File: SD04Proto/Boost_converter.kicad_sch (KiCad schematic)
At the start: 2 parts, among them J1 SL_3.5_2_90G3.2_-1605070000, J2 71308-5410

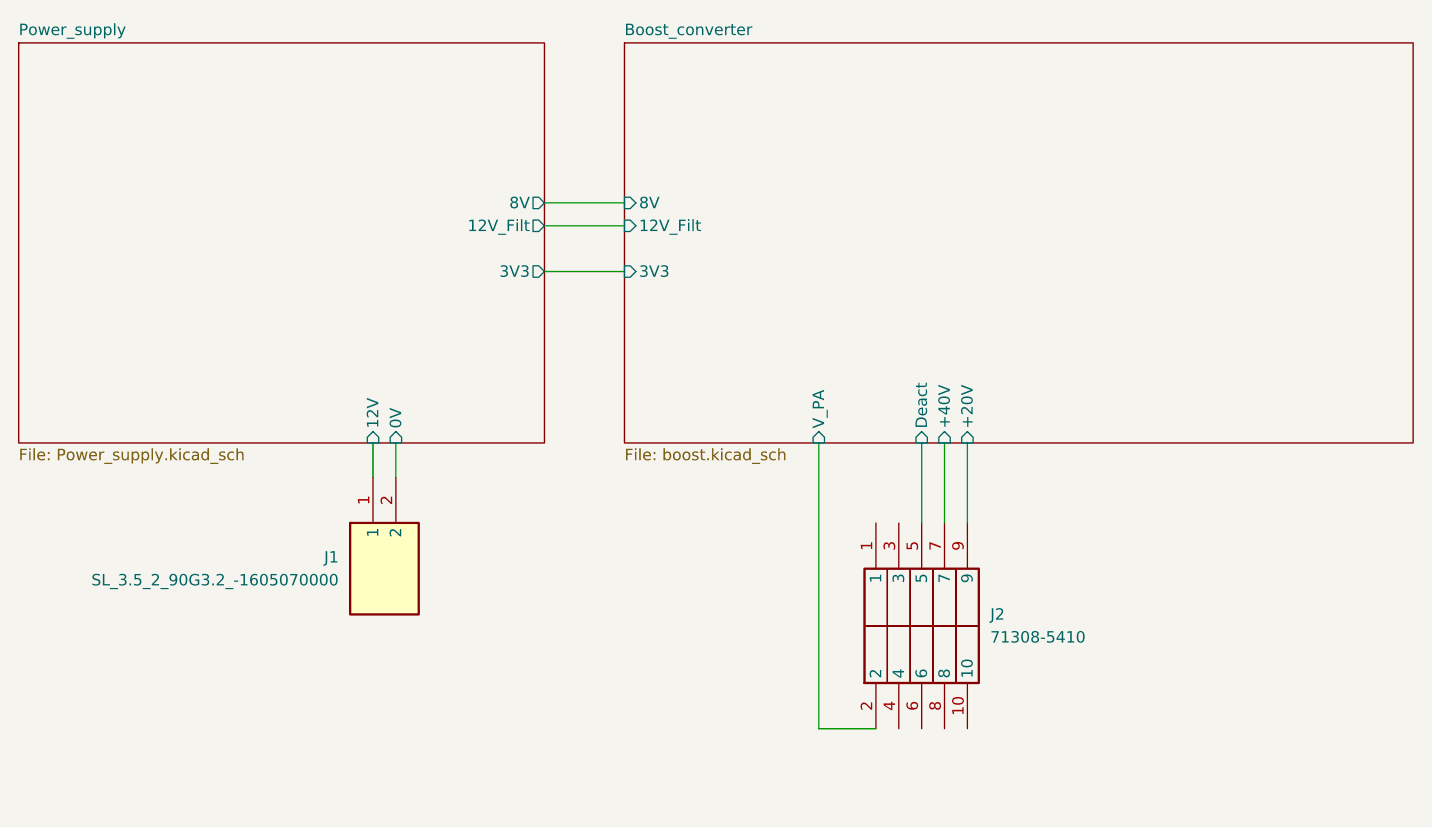
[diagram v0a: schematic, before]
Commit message: changed the layout after review
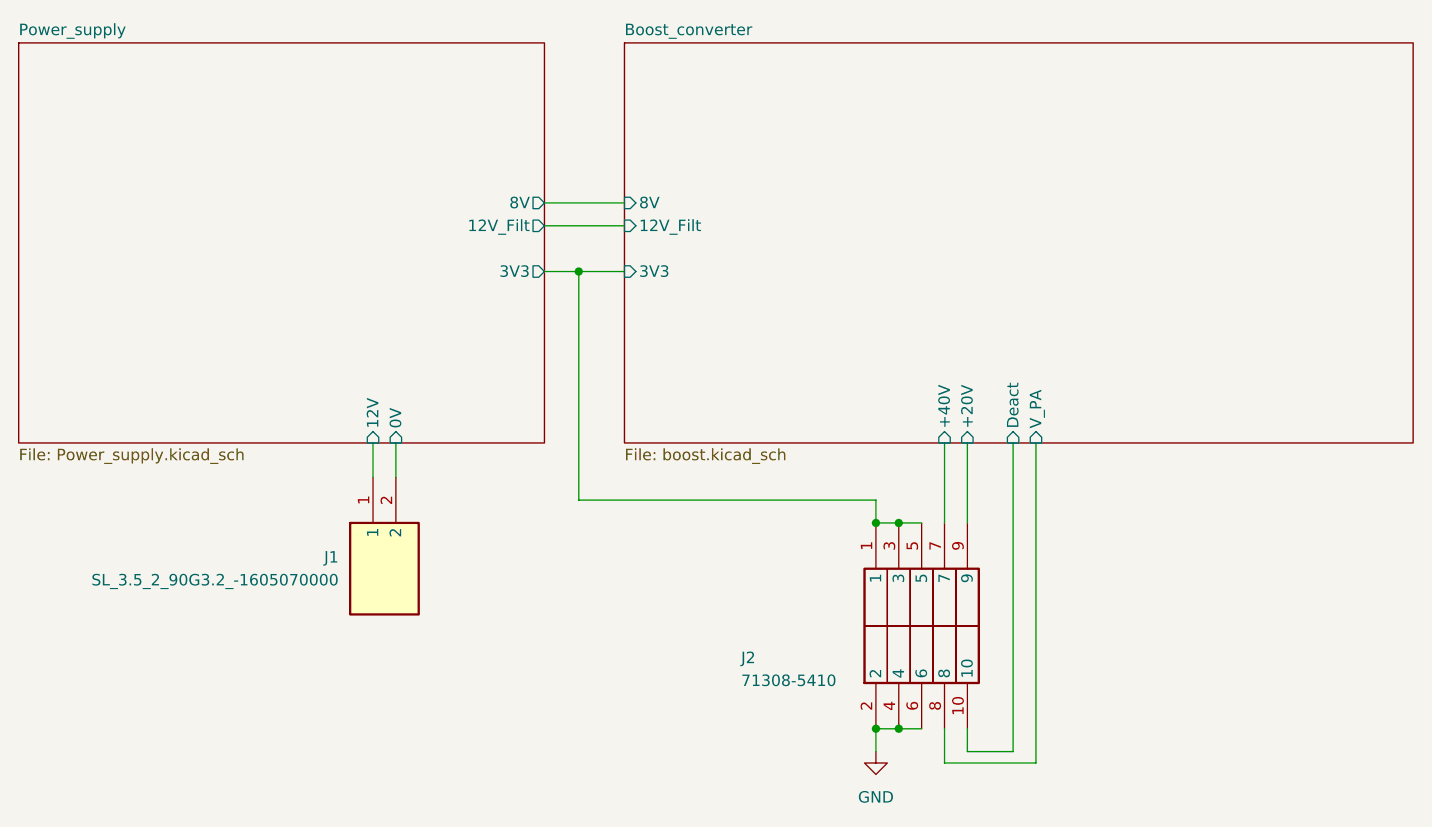
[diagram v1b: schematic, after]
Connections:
- net Boost_converter/3V3: now also J2.1, J2.3, J2.5
- net Boost_converter/Deact: now also J2.10; no longer J2.5
- net Boost_converter/V_PA: now also J2.8; no longer J2.2
- net GND: now reaches J2.4
- net GND: now also J2.2, J2.6
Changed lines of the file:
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@@
 	(generator_version "9.0")
 	(paper "A4")
+	(junction
+		(at 113.03 71.12)
+		(diameter 0)
+		(color 0 0 0 0)
+	)
+	(junction
+		(at 115.57 93.98)
+		(diameter 0)
+		(color 0 0 0 0)
+	)
+	(junction
+		(at 115.57 71.12)
+		(diameter 0)
+		(color 0 0 0 0)
+	)
+	(junction
+		(at 80.01 43.18)
+		(diameter 0)
+		(color 0 0 0 0)
+	)
+	(junction
+		(at 113.03 93.98)
+		(diameter 0)
+		(color 0 0 0 0)
+	)
+	(wire
+		(pts
+			(xy 123.19 96.52) (xy 123.19 93.98)
+		)
+		(stroke
+			(width 0)
+			(type default)
+		)
+	)
+	(wire
+		(pts
+			(xy 115.57 71.12) (xy 118.11 71.12)
+		)
+		(stroke
+			(width 0)
+			(type default)
+		)
+	)
+	(wire
+		(pts
+			(xy 113.03 93.98) (xy 115.57 93.98)
+		)
+		(stroke
+			(width 0)
+			(type default)
+		)
+	)
+	(wire
+		(pts
+			(xy 128.27 96.52) (xy 123.19 96.52)
+		)
+		(stroke
+			(width 0)
+			(type default)
+		)
+	)
+	(wire
+		(pts
+			(xy 113.03 93.98) (xy 113.03 96.52)
+		)
+		(stroke
+			(width 0)
+			(type default)
+		)
+	)
+	(wire
+		(pts
+			(xy 113.03 68.58) (xy 113.03 71.12)
+		)
+		(stroke
+			(width 0)
+			(type default)
+		)
+	)
 	(wire
 		(pts
@@
 	(wire
 		(pts
+			(xy 113.03 68.58) (xy 80.01 68.58)
+		)
+		(stroke
+			(width 0)
+			(type default)
+		)
+	)
+	(wire
+		(pts
+			(xy 115.57 93.98) (xy 118.11 93.98)
+		)
+		(stroke
+			(width 0)
+			(type default)
+		)
+	)
+	(wire
+		(pts
 			(xy 120.65 62.23) (xy 120.65 71.12)
 		)
@@
 	(wire
 		(pts
+			(xy 80.01 68.58) (xy 80.01 43.18)
+		)
+		(stroke
+			(width 0)
+			(type default)
+		)
+	)
+	(wire
+		(pts
+			(xy 113.03 71.12) (xy 115.57 71.12)
+		)
+		(stroke
+			(width 0)
+			(type default)
+		)
+	)
+	(wire
+		(pts
 			(xy 76.2 38.1) (xy 85.09 38.1)
 		)
@@
 	(wire
 		(pts
-			(xy 76.2 43.18) (xy 85.09 43.18)
+			(xy 76.2 43.18) (xy 80.01 43.18)
+		)
+		(stroke
+			(width 0)
+			(type default)
+		)
+	)
+	(wire
+		(pts
+			(xy 120.65 97.79) (xy 120.65 93.98)
 		)
 		(stroke
@@
 	(wire
 		(pts
-			(xy 106.68 93.98) (xy 113.03 93.98)
-		)
-		(stroke
-			(width 0)
-			(type default)
-		)
-	)
-	(wire
-		(pts
-			(xy 118.11 62.23) (xy 118.11 71.12)
-		)
-		(stroke
-			(width 0)
-			(type default)
-		)
-	)
-	(wire
-		(pts
-			(xy 106.68 62.23) (xy 106.68 93.98)
+			(xy 130.81 97.79) (xy 120.65 97.79)
+		)
+		(stroke
+			(width 0)
+			(type default)
+		)
+	)
+	(wire
+		(pts
+			(xy 130.81 62.23) (xy 130.81 97.79)
 		)
 		(stroke
@@
 		(pts
 			(xy 59.69 62.23) (xy 59.69 66.04)
+		)
+		(stroke
+			(width 0)
+			(type default)
+		)
+	)
+	(wire
+		(pts
+			(xy 128.27 62.23) (xy 128.27 96.52)
+		)
+		(stroke
+			(width 0)
+			(type default)
+		)
+	)
+	(wire
+		(pts
+			(xy 80.01 43.18) (xy 85.09 43.18)
 		)
 		(stroke
@@
 	)
 	(symbol
+		(lib_id "power:GND")
+		(at 113.03 96.52 0)
+		(unit 1)
+		(exclude_from_sim no)
+		(in_bom yes)
+		(on_board yes)
+		(dnp no)
+		(fields_autoplaced yes)
+		(property "Reference" "#PWR05"
+			(at 113.03 102.87 0)
+			(effects
+				(font
+					(size 1.27 1.27)
+				)
+				(hide yes)
+			)
+		)
+		(property "Value" "GND"
+			(at 113.03 101.6 0)
+			(effects
+				(font
+					(size 1.27 1.27)
+				)
+			)
+		)
+		(property "Footprint" ""
+			(at 113.03 96.52 0)
+			(effects
+				(font
+					(size 1.27 1.27)
+				)
+				(hide yes)
+			)
+		)
+		(property "Datasheet" ""
+			(at 113.03 96.52 0)
+			(effects
+				(font
+					(size 1.27 1.27)
+				)
+				(hide yes)
+			)
+		)
+		(property "Description" "Power symbol creates a global label with name \"GND\" , ground"
+			(at 113.03 96.52 0)
+			(effects
+				(font
+					(size 1.27 1.27)
+				)
+				(hide yes)
+			)
+		)
+		(pin "1"
+		)
+		(instances
+			(project ""
+				(path "/7f4db626-1185-4eb3-a5a5-b6392b261527"
+					(reference "#PWR05")
+					(unit 1)
+				)
+			)
+		)
+	)
+	(symbol
 		(lib_id "SamacSys_Parts:71308-5410")
 		(at 113.03 93.98 90)
@@
 		(on_board yes)
 		(dnp no)
-		(fields_autoplaced yes)
 		(property "Reference" "J2"
-			(at 125.73 81.2799 90)
+			(at 98.044 86.106 90)
 			(effects
 				(font
@@
 		)
 		(property "Value" "71308-5410"
-			(at 125.73 83.8199 90)
+			(at 98.044 88.646 90)
 			(effects
 				(font
@@
 		)
 		(pin "V_PA" input
-			(at 106.68 62.23 270)
+			(at 130.81 62.23 270)
 			(effects
 				(font
@@
 		)
 		(pin "Deact" input
-			(at 118.11 62.23 270)
-			(effects
-				(font
+			(at 128.27 62.23 270)
+			(effects
+				(font
